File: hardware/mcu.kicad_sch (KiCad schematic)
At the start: 9 parts, among them J3 Link, U1 PGA2350

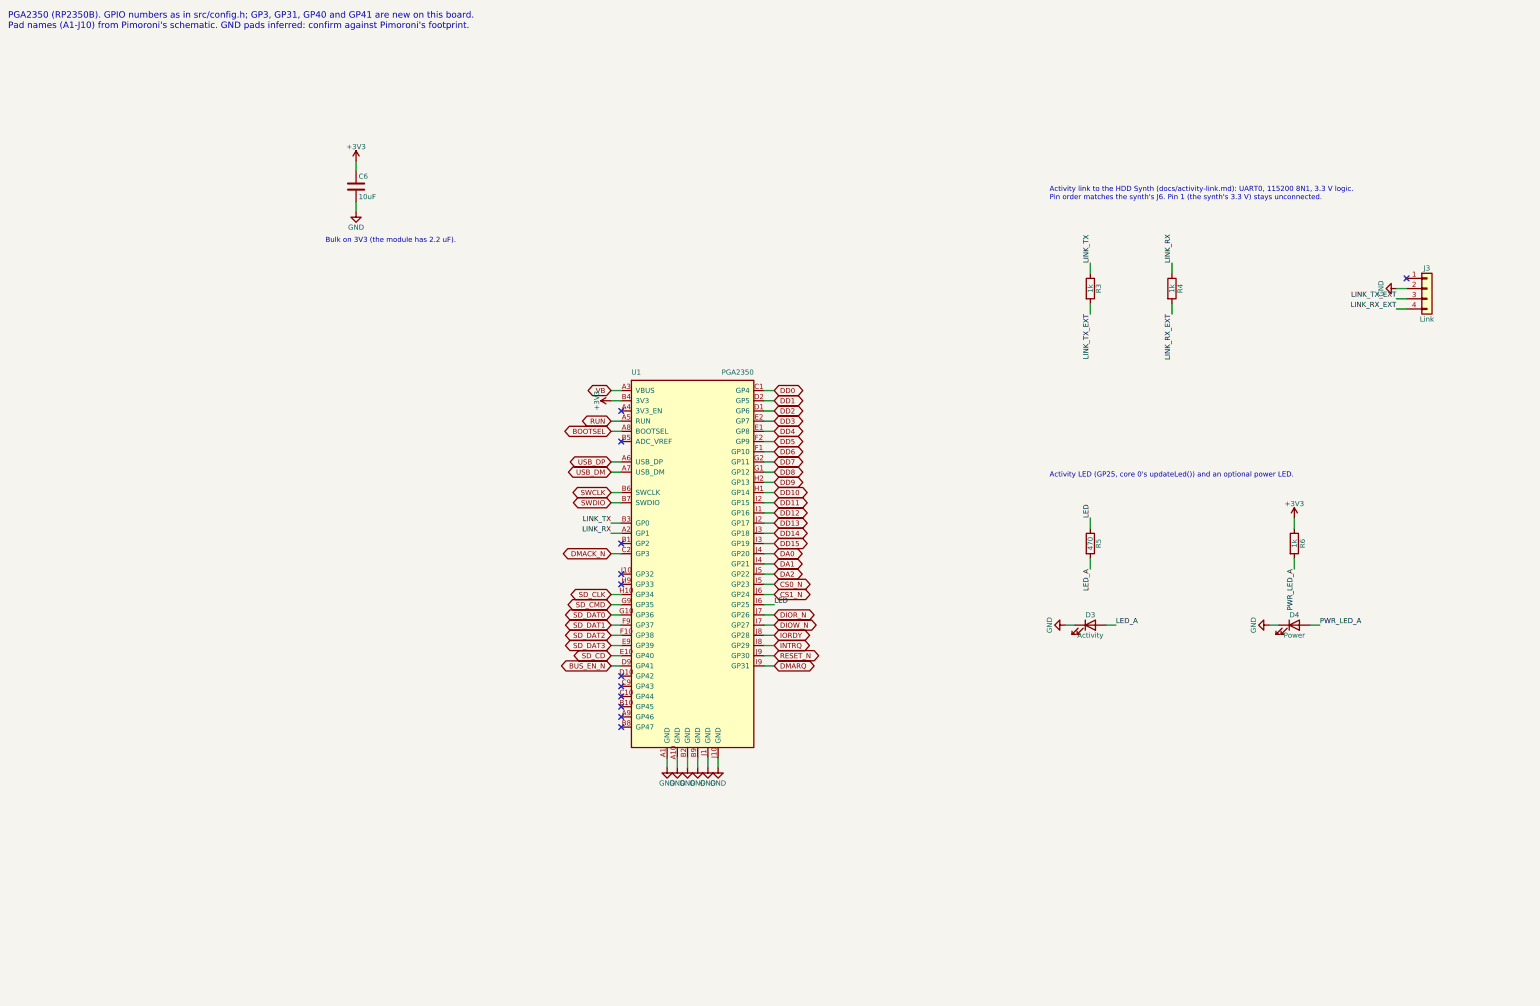
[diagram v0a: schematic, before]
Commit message: PCB rev 0.2: RP2350B on the board instead of the PGA2350 module
The PGA2350 is replaced by an RP2350B with Raspberry Pi's minimal-design
support circuit: their core regulator (polarity-marked inductor), 12 MHz
crystal, W25Q128 flash and USB 27R, with their regulator, QSPI and USB
layout copied relative to the VREG_LX pin; an AMS1117 makes 3V3. GPIO
numbers are unchanged. Supply pins each have a via under the chip.

Cheaper parts from the HDD Synth Mk5: HRO TYPE-C-31-M-12 USB-C, TS-1187A
buttons, and a generic TF PUSH microSD socket. The CB3T3245 bus switches
stay. Every symbol carries its LCSC part number, and Fabrication Toolkit
offsets where JLCPCB's footprint differs from KiCad's; jlcpcb.py applies
the same fitted corrections. check_netlist.py also checks the RP2350
support circuit. ERC and DRC are clean; parts for 5 boards about $68.50.

Co-Authored-By: Claude Opus 5.5 <noreply@anthropic.com>
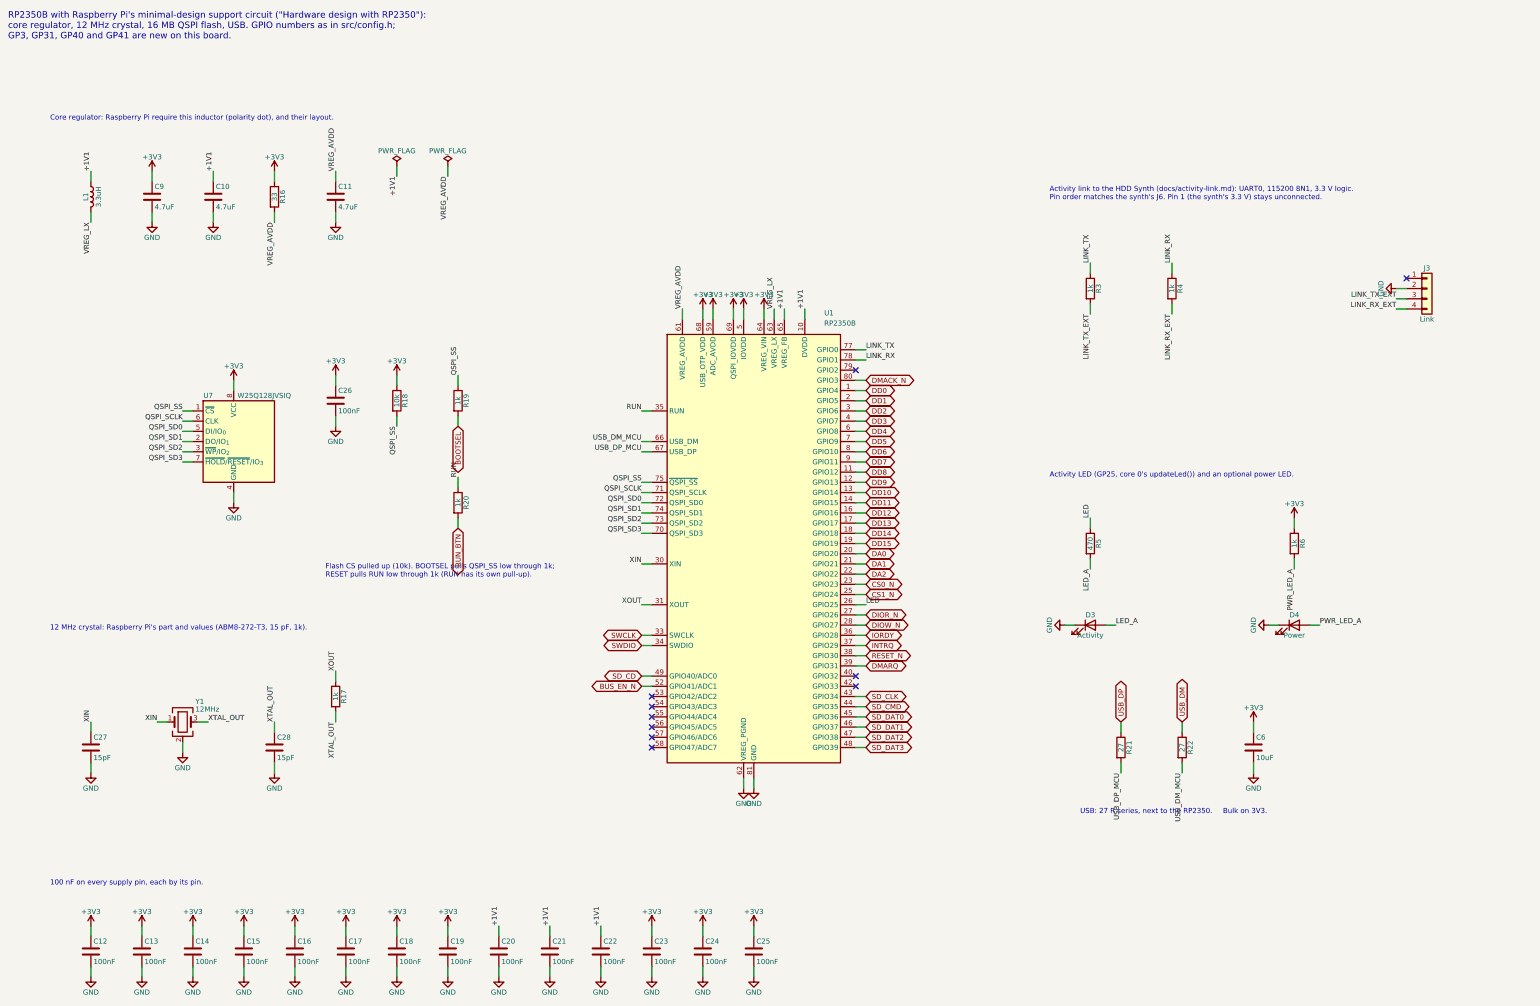
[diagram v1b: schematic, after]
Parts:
- added C10, C9: 4.7uF, HDDSynthPro:C_0402_1005Metric_RPi_Wide, symbol Device:C
- added C11: 4.7uF, Capacitor_SMD:C_0402_1005Metric, symbol Device:C
- added C12, C13, C14, C15, C16, C17, C18, C19, C20, C21, C22, C23, C24, C25, C26: 100nF, Capacitor_SMD:C_0402_1005Metric, symbol Device:C
- added C27, C28: 15pF, Capacitor_SMD:C_0402_1005Metric, symbol Device:C
- added L1: 3.3uH, HDDSynthPro:L_Abracon_AOTA-B201610S3R3, symbol Device:L
- added R16: 33, Resistor_SMD:R_0402_1005Metric, symbol Device:R
- added R17, R19: 1k, Resistor_SMD:R_0402_1005Metric, symbol Device:R
- added R18: 10k, Resistor_SMD:R_0402_1005Metric, symbol Device:R
- added R20: 1k, Resistor_SMD:R_0603_1608Metric, symbol Device:R
- added R21, R22: 27, Resistor_SMD:R_0402_1005Metric, symbol Device:R
- added U7: W25Q128JVSIQ, Package_SO:SOIC-8_5.3x5.3mm_P1.27mm, symbol Memory_Flash:W25Q128JVS
- added Y1: 12MHz, Crystal:Crystal_SMD_3225-4Pin_3.2x2.5mm, symbol Device:Crystal_GND24
- C6: LCSC (none) -> C15850
- D3: LCSC (none) -> C2297
- D4: LCSC (none) -> C84256
- J3: FT Rotation Offset (none) -> -90; LCSC (none) -> C2718488
- R3, R4, R6: LCSC (none) -> C21190
- R5: LCSC (none) -> C23179
- U1: value PGA2350 -> RP2350B; footprint HDDSynthPro:PGA2350 -> Package_DFN_QFN:QFN-80-1EP_10x10mm_P0.4mm_EP3.4x3.4mm_ThermalVias; symbol HDDSynthPro:PGA2350 -> MCU_RaspberryPi:RP2350B; FT Rotation Offset (none) -> -90; LCSC (none) -> C42415655; MPN Pimoroni PIM722 -> (none)
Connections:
- net +3V3: now also U1.15 (IOVDD), U1.24 (IOVDD), U1.29 (IOVDD), U1.41 (IOVDD), U1.5 (IOVDD), U1.50 (IOVDD), U1.59 (ADC_AVDD), U1.60 (IOVDD), U1.64 (VREG_VIN), U1.68 (USB_OTP_VDD), U1.69 (QSPI_IOVDD), U1.76 (IOVDD), C12.1, C13.1, C14.1, C15.1, C16.1, C17.1, C18.1, C19.1, C23.1, C24.1, C25.1, C26.1, C9.1, R16.1, R18.1, U7.8 (VCC); no longer U1.B4 (3V3)
- net BOOTSEL: now also R19.2; no longer U1.A8 (BOOTSEL)
- net BUS_EN_N: now also U1.52 (GPIO41/ADC1); no longer U1.D9 (GP41)
- net CS0_N: now also U1.23 (GPIO23); no longer U1.I5 (GP23)
- net CS1_N: now also U1.25 (GPIO24); no longer U1.J6 (GP24)
- net DA0: now also U1.20 (GPIO20); no longer U1.J4 (GP20)
- net DA1: now also U1.21 (GPIO21); no longer U1.I4 (GP21)
- net DA2: now also U1.22 (GPIO22); no longer U1.J5 (GP22)
- net DD0: now also U1.1 (GPIO4); no longer U1.C1 (GP4)
- net DD1: now also U1.2 (GPIO5); no longer U1.D2 (GP5)
- net DD10: now also U1.13 (GPIO14); no longer U1.H1 (GP14)
- net DD11: now also U1.14 (GPIO15); no longer U1.I2 (GP15)
- net DD12: now also U1.16 (GPIO16); no longer U1.I1 (GP16)
- net DD13: now also U1.17 (GPIO17); no longer U1.J2 (GP17)
- net DD14: now also U1.18 (GPIO18); no longer U1.J3 (GP18)
- net DD15: now also U1.19 (GPIO19); no longer U1.I3 (GP19)
- net DD2: now also U1.3 (GPIO6); no longer U1.D1 (GP6)
- net DD3: now also U1.4 (GPIO7); no longer U1.E2 (GP7)
- net DD4: now also U1.6 (GPIO8); no longer U1.E1 (GP8)
- net DD5: now also U1.7 (GPIO9); no longer U1.F2 (GP9)
- net DD6: now also U1.8 (GPIO10); no longer U1.F1 (GP10)
- net DD7: now also U1.9 (GPIO11); no longer U1.G2 (GP11)
- net DD8: now also U1.11 (GPIO12); no longer U1.G1 (GP12)
- net DD9: now also U1.12 (GPIO13); no longer U1.H2 (GP13)
- net DIOR_N: now also U1.27 (GPIO26); no longer U1.J7 (GP26)
- net DIOW_N: now also U1.28 (GPIO27); no longer U1.I7 (GP27)
- net DMACK_N: now also U1.80 (GPIO3); no longer U1.C2 (GP3)
- net DMARQ: now also U1.39 (GPIO31); no longer U1.I9 (GP31)
- net GND: now also U1.62 (VREG_PGND), U1.81 (GND), C10.2, C11.2, C12.2, C13.2, C14.2, C15.2, C16.2, C17.2, C18.2, C19.2, C20.2, C21.2, C22.2, C23.2, C24.2, C25.2, C26.2, C27.2, C28.2, C9.2, U7.4 (GND), Y1.2 (G), Y1.4 (G); no longer U1.A1 (GND), U1.A10 (GND), U1.B2 (GND), U1.B9 (GND), U1.J1 (GND), U1.J10 (GND)
- net INTRQ: now also U1.37 (GPIO29); no longer U1.I8 (GP29)
- net IORDY: now also U1.36 (GPIO28); no longer U1.J8 (GP28)
- net LED: now also U1.26 (GPIO25); no longer U1.I6 (GP25)
- net LINK_RX: now also U1.78 (GPIO1); no longer U1.A2 (GP1)
- net LINK_TX: now also U1.77 (GPIO0); no longer U1.B3 (GP0)
- net RESET_N: now also U1.38 (GPIO30); no longer U1.J9 (GP30)
- net RUN: now also U1.35 (RUN), R20.1; no longer U1.A5 (RUN)
- net SD_CD: now also U1.49 (GPIO40/ADC0); no longer U1.E10 (GP40)
- net SD_CLK: now also U1.43 (GPIO34); no longer U1.H10 (GP34)
- net SD_CMD: now also U1.44 (GPIO35); no longer U1.G9 (GP35)
- net SD_DAT0: now also U1.45 (GPIO36); no longer U1.G10 (GP36)
- net SD_DAT1: now also U1.46 (GPIO37); no longer U1.F9 (GP37)
- net SD_DAT2: now also U1.47 (GPIO38); no longer U1.F10 (GP38)
- net SD_DAT3: now also U1.48 (GPIO39); no longer U1.E9 (GP39)
- net SWCLK: now also U1.33 (SWCLK); no longer U1.B6 (SWCLK)
- net SWDIO: now also U1.34 (SWDIO); no longer U1.B7 (SWDIO)
- net USB_DM: now also R22.1; no longer U1.A7 (USB_DM)
- net USB_DP: now also R21.1; no longer U1.A6 (USB_DP)
- removed net VB: U1.A3 (VBUS)
- new net +1V1: C10.1, C20.1, C21.1, C22.1, L1.1, U1.10 (DVDD), U1.32 (DVDD), U1.51 (DVDD), U1.65 (VREG_FB)
- new net QSPI_SCLK: U1.71 (QSPI_SCLK), U7.6 (CLK)
- new net QSPI_SD0: U1.72 (QSPI_SD0), U7.5 (DI/IO_{0})
- new net QSPI_SD1: U1.74 (QSPI_SD1), U7.2 (DO/IO_{1})
- new net QSPI_SD2: U1.73 (QSPI_SD2), U7.3 (~{WP}/IO_{2})
- new net QSPI_SD3: U1.70 (QSPI_SD3), U7.7 (~{HOLD}/~{RESET}/IO_{3})
- new net QSPI_SS: R18.2, R19.1, U1.75 (~{QSPI_SS}), U7.1 (~{CS})
- new net RUN_BTN: R20.2
- new net USB_DM_MCU: R22.2, U1.66 (USB_DM)
- new net USB_DP_MCU: R21.2, U1.67 (USB_DP)
- new net VREG_AVDD: C11.1, R16.2, U1.61 (VREG_AVDD)
- new net VREG_LX: L1.2, U1.63 (VREG_LX)
- new net XIN: C27.1, U1.30 (XIN), Y1.1
- new net XOUT: R17.1, U1.31 (XOUT)
- new net XTAL_OUT: C28.1, R17.2, Y1.3
- no-connect marks 12 -> 10
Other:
- note added: "100 nF on every supply pin, each by its pin."
- note added: "12 MHz crystal: Raspberry Pi's part and values (ABM8-272-T3, 15 pF, 1k)."
- note added: "Bulk on 3V3."
- note added: "Core regulator: Raspberry Pi require this inductor (polarity dot), and their layout."
- note added: "Flash CS pulled up (10k). BOOTSEL pulls QSPI_SS low through 1k; RESET pulls RUN low through 1k (RUN has its own pull-up)."
- note added: "RP2350B with Raspberry Pi's minimal-design support circuit ("Hardware design with RP2350"): core regulator, 12 MHz crystal, 16 MB QSPI flash, USB. GPIO numbers as in src/config.h; GP3, GP31, GP40 and GP41 are new on this board."
- note added: "USB: 27 R series, next to the RP2350."
- note removed: "Bulk on 3V3 (the module has 2.2 uF)."
- note removed: "PGA2350 (RP2350B). GPIO numbers as in src/config.h; GP3, GP31, GP40 and GP41 are new on this board. Pad names (A1-J10) from Pimoroni's schematic. GND pads inferred: confirm against Pimoroni's footprint."
- title: HDDSynthPro: PGA2350 -> HDDSynthPro: RP2350
- moved on the sheet: C6

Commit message: PCB rev 0.3: HDD Synth Mk5 outline and holes, 5 V in on the link socket
- The board takes the Mk5's outline (100.33 x 69.88 mm, 2.54 mm corners)
  and its four M3 holes, so the two boards stack on standoffs. The IDE
  header moves inside the left-hand holes; everything else shifts right.
  The logo still fits on the front.
- J3 pin 1 takes 5 V from the HDD Synth through D5 (SS14) into VB, beside
  USB and the 5 V header, so one supply can run both boards. The Mk5's J6
  pin 1 is 3.3 V, so leave it unconnected with a Mk5.
- check_netlist.py checks the new input; rerouted with Freerouting: ERC 0,
  DRC 0 errors, 0 unconnected, 0 parity issues.

Co-Authored-By: Claude Opus 5.5 <noreply@anthropic.com>
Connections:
- net 5V_LINK: now reaches J3.1 (Pin_1)
- no-connect marks 10 -> 9
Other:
- note added: "Activity link to the HDD Synth (docs/activity-link.md): UART0, 115200 8N1, 3.3 V logic. Pin order matches the synth's J6. Pin 1 takes 5 V from the synth, through D5 (Power and USB sheet), so one supply runs both boards. The synth's J6 pin 1 must carry 5 V, not its 3.3 V."
- note removed: "Activity link to the HDD Synth (docs/activity-link.md): UART0, 115200 8N1, 3.3 V logic. Pin order matches the synth's J6. Pin 1 (the synth's 3.3 V) stays unconnected."
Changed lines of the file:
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@@
 	(title_block
 		(title "HDDSynthPro: RP2350")
-		(date "2026-10-26")
-		(rev "0.1")
+		(date "2026-10-27")
+		(rev "0.3")
 		(company "HDDSynthPro")
 		(comment 1 "Generated by hardware/tools/gen_schematic.py from docs/pcb.html")
@@
 		)
 	)
-	(text "Activity link to the HDD Synth (docs/activity-link.md): UART0, 115200 8N1, 3.3 V logic.\nPin order matches the synth's J6. Pin 1 (the synth's 3.3 V) stays unconnected."
+	(text "Activity link to the HDD Synth (docs/activity-link.md): UART0, 115200 8N1, 3.3 V logic.\nPin order matches the synth's J6. Pin 1 takes 5 V from the synth, through D5 (Power and USB sheet),\nso one supply runs both boards. The synth's J6 pin 1 must carry 5 V, not its 3.3 V."
 		(exclude_from_sim no)
 		(at 279.4 63.5 0)
@@
 		)
 	)
-	(no_connect
-		(at 368.3 86.36)
+	(wire
+		(pts
+			(xy 368.3 86.36)
+			(xy 365.76 86.36)
+		)
+		(stroke
+			(width 0)
+			(type default)
+		)
 	)
 	(wire
@@
 		)
 	)
+	(global_label "5V_LINK"
+		(shape bidirectional)
+		(at 365.76 86.36 180)
+		(fields_autoplaced yes)
+		(effects
+			(font
+				(size 1.27 1.27)
+			)
+			(justify right)
+		)
+		(property "Intersheetrefs" "${INTERSHEET_REFS}"
+			(at 365.76 86.36 180)
+			(effects
+				(font
+					(size 1.27 1.27)
+				)
+				(justify right)
+				(hide yes)
+			)
+		)
+	)
